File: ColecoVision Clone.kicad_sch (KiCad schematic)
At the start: 17 parts, among them J1 Cartridge Slot, U1 PLCCZ80, U100 AS6C62256-DIP, U12 74LS138 (Mem. Mapped), U13 74LS138 (I/O), U14 74LS02, U3 BIOS ROM 27C256

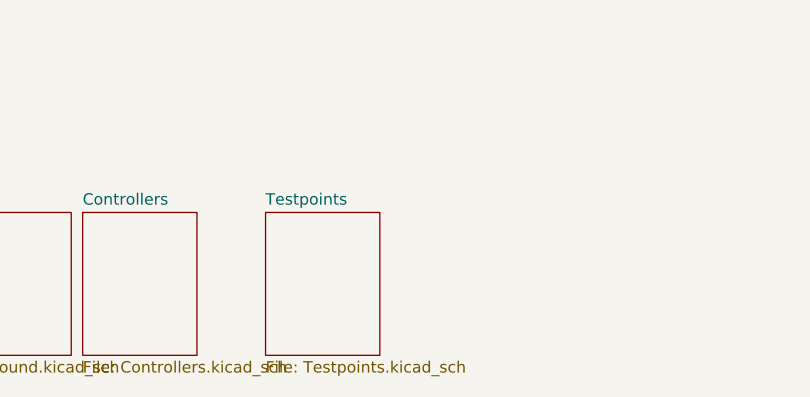
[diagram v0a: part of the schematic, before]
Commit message: Get rid of old Testpoints schematic
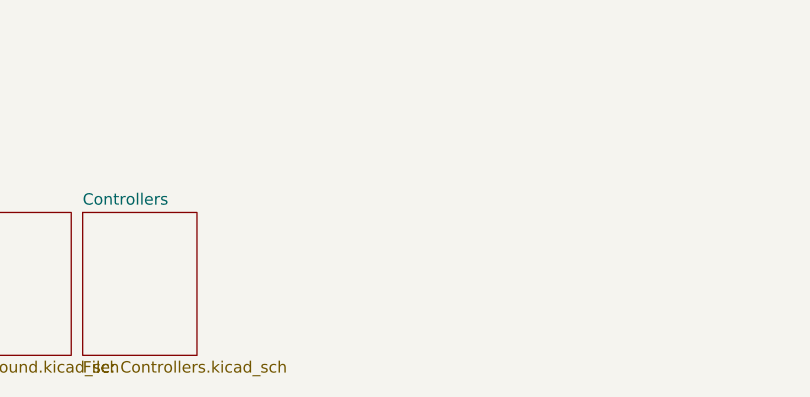
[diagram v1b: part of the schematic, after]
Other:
- removed sheet Testpoints
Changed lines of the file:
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@@
-    )
-  )
-  (sheet (at 106.68 172.085) (size 12.7 15.875) (fields_autoplaced)
-    (stroke (width 0) (type solid) (color 0 0 0 0))
-    (fill (color 0 0 0 0.0000))
-    (property "Sheet name" "Testpoints" (id 0) (at 106.68 171.3734 0)
-      (effects (font (size 1.27 1.27)) (justify left bottom))
-    )
-    (property "Sheet file" "Testpoints.kicad_sch" (id 1) (at 106.68 188.5446 0)
-      (effects (font (size 1.27 1.27)) (justify left top))
     )
   )
@@
     (path "/00000000-0000-0000-0000-00005e3c7714" (page "5"))
     (path "/00000000-0000-0000-0000-00005e40fc69" (page "6"))
-    (path "/00000000-0000-0000-0000-00005e40230d" (page "7"))
   )
   (symbol_instances
